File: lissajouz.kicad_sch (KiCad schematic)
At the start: 105 parts, among them J1 Barrel_Jack, Q1 BC557, Q10 2N7000, Q2 BC557, Q3 2N7000, Q4 BC557, Q5 BC557, Q6 2N7000, Q7 2N7000, Q8 2N7000, Q9 2N7000, U1 LM324, U2 LM324, U3 LM324

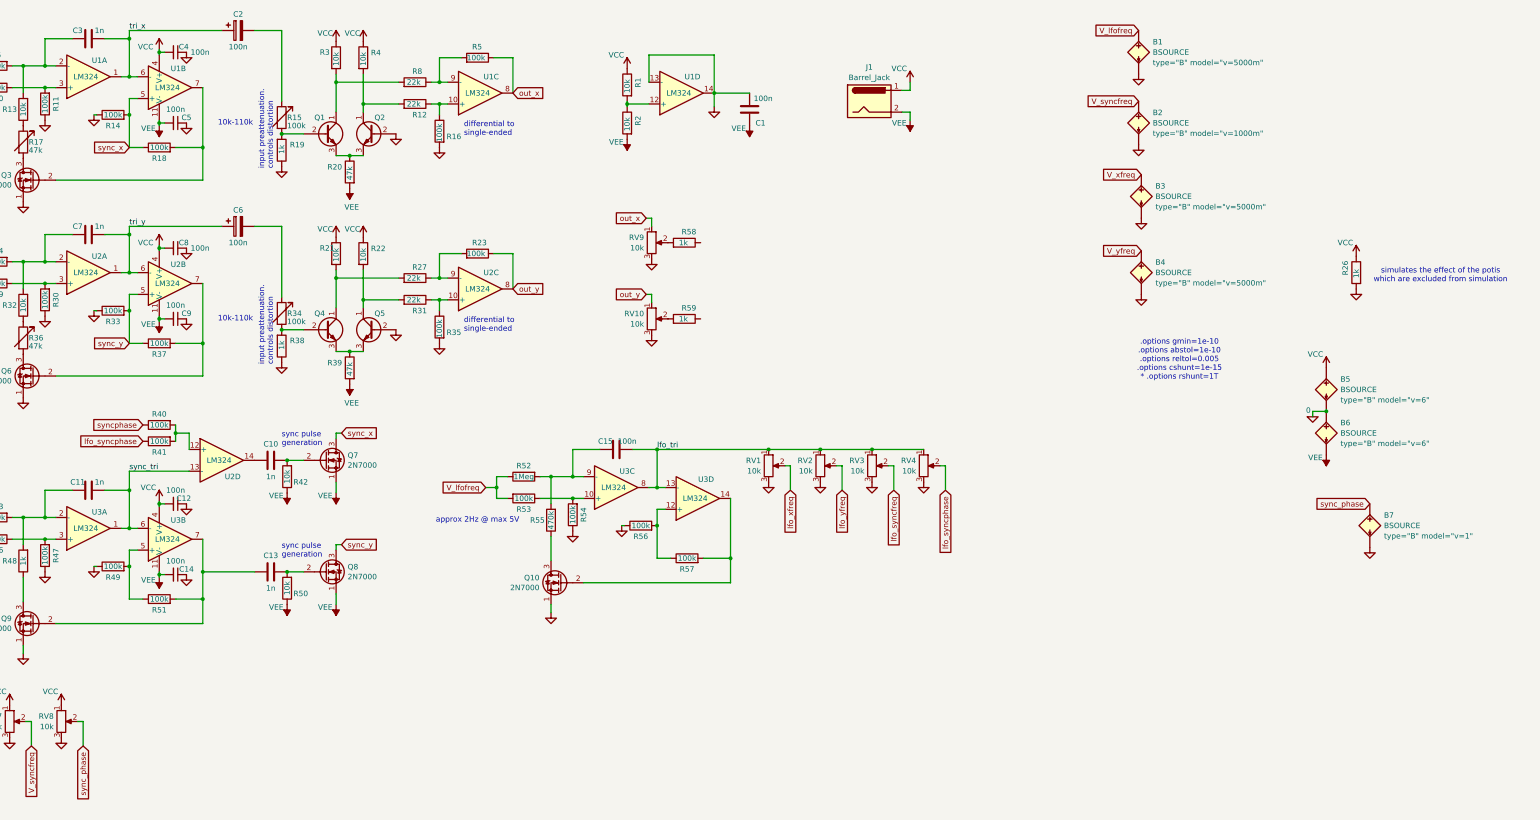
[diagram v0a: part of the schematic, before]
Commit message: add most footprints
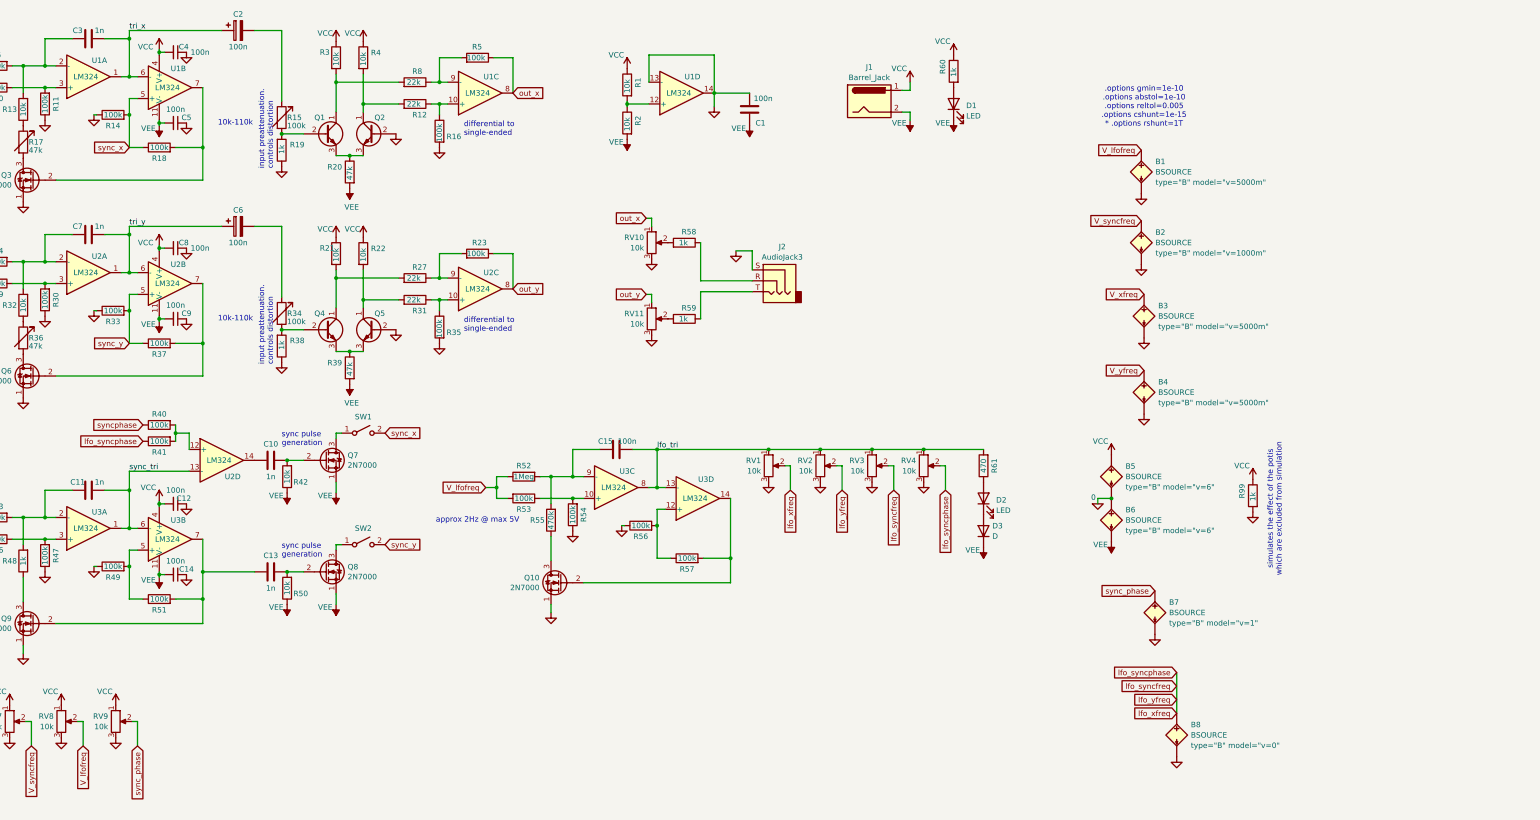
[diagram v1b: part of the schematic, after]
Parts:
- added B8: BSOURCE, symbol Simulation_SPICE:BSOURCE
- added D1, D2: LED, LED_THT:LED_D3.0mm, symbol Device:LED
- added D3: D, Diode_THT:D_5W_P5.08mm_Vertical_AnodeUp, symbol Device:D
- added J2: AudioJack3, symbol Connector_Audio:AudioJack3
- added R60: 1k, Resistor_SMD:R_0805_2012Metric_Pad1.20x1.40mm_HandSolder, symbol Device:R
- added R61: 470, Resistor_SMD:R_0805_2012Metric_Pad1.20x1.40mm_HandSolder, symbol Device:R
- added RV9: 10k, Potentiometer_THT:Potentiometer_Alpha_RD901F-40-00D_Single_Vertical, symbol Device:R_Potentiometer
- added SW1, SW2: ${SIM.PARAMS}, symbol Switch:SW_SPST
- C1, C10, C11, C12, C13, C14, C15, C3, C4, C5, C7, C8, C9: footprint Capacitor_SMD:C_0805_2012Metric_Pad1.15x1.40mm_HandSolder -> Capacitor_SMD:C_0805_2012Metric_Pad1.18x1.45mm_HandSolder
- C2, C6: footprint Capacitor_THT:CP_Radial_D7.5mm_P2.50mm -> Capacitor_SMD:C_0805_2012Metric_Pad1.18x1.45mm_HandSolder
- J1: footprint (none) -> Connector_BarrelJack:BarrelJack_SwitchcraftConxall_RAPC10U_Horizontal
- R1, R10, R11, R12, R13, R14, R16, R18, R19, R2, R20, R21, R22, R23, R24, R25, R27, R28, R29, R3, R30, R31, R32, R33, R35, R37, R38, R39, R4, R40, R41, R42, R43, R44, R45, R46, R47, R48, R49, R5, R50, R51, R52, R53, R54, R55, R56, R57, R58, R59, R6, R7, R8, R9: footprint Resistor_SMD:R_0805_2012Metric_Pad1.15x1.40mm_HandSolder -> Resistor_SMD:R_0805_2012Metric_Pad1.20x1.40mm_HandSolder
- R15, R34: footprint Potentiometer_THT:Potentiometer_Runtron_RM-065_Vertical -> Potentiometer_THT:Potentiometer_Alpha_RD901F-40-00D_Single_Vertical
- R17, R36: footprint Potentiometer_THT:Potentiometer_Runtron_RM-065_Vertical -> Resistor_SMD:R_0805_2012Metric_Pad1.20x1.40mm_HandSolder
- RV1, RV2, RV3, RV4, RV5, RV6, RV7, RV8: footprint (none) -> Potentiometer_THT:Potentiometer_Alpha_RD901F-40-00D_Single_Vertical
- RV10: renamed from RV9; footprint (none) -> Potentiometer_THT:Potentiometer_Runtron_RM-065_Vertical
- RV11: renamed from RV10; footprint (none) -> Potentiometer_THT:Potentiometer_Runtron_RM-065_Vertical
- renumbered R26 to R99
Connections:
- net lfo_syncphase is gone; now on net lfo_syncfreq: R41.1, RV4.2
- net lfo_xfreq is gone; now on net lfo_syncfreq: R9.1, RV1.2
- net lfo_yfreq is gone; now on net lfo_syncfreq: R28.1, RV2.2
- net GNDREF: now also B8.2 (N-), J2.S, RV9.3
- net VCC: now also R60.1, RV9.1
- net VEE: now also D1.1 (K), D3.1 (K)
- net V_lfofreq: now also RV8.2
- net lfo_syncfreq: now also B8.1 (N+)
- net lfo_tri: now also R61.2
- net sync_phase: now also RV9.2; no longer RV8.2
- net sync_x: now also SW1.2 (B); no longer Q7.3 (D)
- net sync_y: now also SW2.2 (B); no longer Q8.3 (D)
- net at R59.1: now also J2.T
- net at R58.1: now also J2.R
- new net: D2.1 (K), D3.2 (A)
- new net: D2.2 (A), R61.1
- new net: Q7.3 (D), SW1.1 (A)
- new net: Q8.3 (D), SW2.1 (A)
- new net: D1.2 (A), R60.2
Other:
- moved on the sheet: B1, B2, B3, B4, B5, B6, B7, R99

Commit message: pcb
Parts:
- R17, R36: footprint Resistor_SMD:R_0805_2012Metric_Pad1.20x1.40mm_HandSolder -> Potentiometer_THT:Potentiometer_Alpha_RD901F-40-00D_Single_Vertical
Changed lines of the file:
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@@
 			)
 		)
-		(property "Footprint" "Resistor_SMD:R_0805_2012Metric_Pad1.20x1.40mm_HandSolder"
+		(property "Footprint" "Potentiometer_THT:Potentiometer_Alpha_RD901F-40-00D_Single_Vertical"
 			(at 48.387 86.995 90)
 			(effects
@@
 			)
 		)
-		(property "Footprint" "Resistor_SMD:R_0805_2012Metric_Pad1.20x1.40mm_HandSolder"
+		(property "Footprint" "Potentiometer_THT:Potentiometer_Alpha_RD901F-40-00D_Single_Vertical"
 			(at 48.387 41.275 90)
 			(effects

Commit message: kinda final-ish UI layout
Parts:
- added R26, R62: 100k, Resistor_SMD:R_0805_2012Metric_Pad1.20x1.40mm_HandSolder, symbol Device:R
- added R63, R64, R65: 1k, Resistor_SMD:R_0805_2012Metric_Pad1.20x1.40mm_HandSolder, symbol Device:R
- added R66: 2.2k, Resistor_SMD:R_0805_2012Metric_Pad1.20x1.40mm_HandSolder, symbol Device:R
- added R67, R68: 4.7k, Resistor_SMD:R_0805_2012Metric_Pad1.20x1.40mm_HandSolder, symbol Device:R
- added R69: 1Meg, Resistor_SMD:R_0805_2012Metric_Pad1.20x1.40mm_HandSolder, symbol Device:R
- added RV12, RV13, RV14: 10k, Potentiometer_THT:Potentiometer_Alpha_RD901F-40-00D_Single_Vertical, symbol Device:R_Potentiometer
- J1: footprint Connector_BarrelJack:BarrelJack_SwitchcraftConxall_RAPC10U_Horizontal -> footprints:myBarrelJack
- J2: footprint (none) -> Connector_Audio:Jack_3.5mm_CUI_SJ1-3535NG_Horizontal
- SW1, SW2: footprint (none) -> footprints:switch8x8
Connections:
- net syncphase is gone; now on net sync_phase: R40.1
- net GNDREF: now also R63.1, R64.1, R65.1, R66.1, RV12.3, RV13.3; no longer RV5.3, RV6.3, RV7.3, RV8.3, RV9.3
- net VCC: now also R67.2, RV12.1, RV13.1, RV14.1; no longer RV9.1
- net VEE: now also R68.1, RV14.3
- net at R40.2, R41.2, U2.12 (+): now also R69.2
- net at R24.1, R25.2, R28.2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: now also R62.2
- net at R10.2, R6.1, R7.2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: now also R26.2
- new net: R64.2, RV6.3
- new net: R67.1, RV9.1
- new net: R68.2, RV9.3
- new net: R66.2, RV8.3
- new net: R65.2, RV7.3
- new net: R63.2, RV5.3
- new net V_xfreq_fine: R26.1, RV12.2
- new net V_yfreq_fine: R62.1, RV13.2
- new net sync_phase_fine: R69.1, RV14.2
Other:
- moved on the sheet: R25, R28, R40, R7, R9, RV7, RV8, RV9

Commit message: all components positioned
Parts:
- added B10, B11, B9: BSOURCE, symbol Simulation_SPICE:BSOURCE
- D3: footprint Diode_THT:D_5W_P5.08mm_Vertical_AnodeUp -> Diode_THT:D_5W_P12.70mm_Horizontal
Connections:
- net GNDREF is gone; now on net GND: B1.2 (N-), B2.2 (N-), B3.2 (N-), B4.2 (N-), B7.2 (N-), B8.2 (N-), C1.1, C12.1, C14.1, C4.1, C5.1, C8.1, C9.1, J2.S, Q10.1 (S), Q3.1 (S), Q6.1 (S), Q9.1 (S), R11.1, R14.1, R30.1, R33.1, R47.1, R49.1, R54.1, R56.1, R63.1, R64.1, R65.1, R66.1, R99.2, RV1.3, RV10.3, RV11.3, RV12.3, RV13.3, RV2.3, RV3.3, RV4.3, U1.13 (-), U1.14
- net GND: now also B10.2 (N-), B11.2 (N-), B9.2 (N-)
- net V_xfreq: now also R25.1; no longer R7.1
- net V_xfreq_fine: now also R62.1; no longer R26.1
- net V_yfreq: now also R7.1; no longer R25.1
- net V_yfreq_fine: now also R26.1; no longer R62.1
- net lfo_syncfreq: now also B10.1 (N+); no longer B8.1 (N+), R28.1, R41.1, R9.1, RV1.2, RV2.2, RV4.2
- net lfo_tri: now also U3.6 (-); no longer U3.13 (-)
- net out_x: now also R23.1, U2.8; no longer R5.1, U1.8
- net out_y: now also R5.1, U1.8; no longer R23.1, U2.8
- net sync_tri: now also U3.13 (-); no longer U3.6 (-)
- net sync_x: now also R33.2, R37.1, U2.5 (+); no longer R14.2, R18.1, U1.5 (+)
- net sync_y: now also R14.2, R18.1, U1.5 (+); no longer R33.2, R37.1, U2.5 (+)
- net tri_x: now also C6.1, C7.1, U2.1, U2.6 (-); no longer C2.1, C3.1, U1.1, U1.6 (-)
- net tri_y: now also C2.1, C3.1, U1.1, U1.6 (-); no longer C6.1, C7.1, U2.1, U2.6 (-)
- net at R49.2, R51.1: now also U3.12 (+); no longer U3.5 (+)
- net at C13.2, Q9.2 (G), R51.2: now also U3.14; no longer U3.7
- net at R56.2, R57.1: now also U3.5 (+); no longer U3.12 (+)
- net at Q10.2 (G), R57.2: now also U3.7; no longer U3.14
- new net lfo_syncphase: B11.1 (N+), R41.1, RV4.2
- new net lfo_xfreq: B8.1 (N+), R28.1, RV1.2
- new net lfo_yfreq: B9.1 (N+), R9.1, RV2.2
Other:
- moved on the sheet: B8

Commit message: frontplate++
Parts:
- added R70, R71: 10k, Resistor_SMD:R_0805_2012Metric_Pad1.20x1.40mm_HandSolder, symbol Device:R
- R15, R17, R34, R36, RV1, RV12, RV13, RV14, RV2, RV3, RV4, RV5, RV6, RV7, RV8, RV9: footprint Potentiometer_THT:Potentiometer_Alpha_RD901F-40-00D_Single_Vertical -> footprints:my_poti_Potentiometer_Alpha_RD901F-40-00D_Single_Vertical
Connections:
- net at C6.2: now also R71.2; no longer R34.1
- net at R15.1: now also R70.1; no longer C2.2
- new net: C2.2, R70.2
- new net: R34.1, R71.1
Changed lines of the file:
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@@
 	(wire
 		(pts
-			(xy 110.49 15.24) (xy 110.49 31.75)
-		)
-		(stroke
-			(width 0)
-			(type default)
-		)
-	)
-	(wire
-		(pts
 			(xy 229.235 122.555) (xy 229.235 116.84)
 		)
@@
 	(wire
 		(pts
+			(xy 110.49 15.24) (xy 110.49 24.13)
+		)
+		(stroke
+			(width 0)
+			(type default)
+		)
+	)
+	(wire
+		(pts
 			(xy 61.595 62.865) (xy 55.245 62.865)
 		)
@@
 	(wire
 		(pts
+			(xy 110.49 60.96) (xy 110.49 69.85)
+		)
+		(stroke
+			(width 0)
+			(type default)
+		)
+	)
+	(wire
+		(pts
 			(xy 229.235 116.84) (xy 227.965 116.84)
 		)
@@
 	(wire
 		(pts
-			(xy 110.49 60.96) (xy 110.49 77.47)
-		)
-		(stroke
-			(width 0)
-			(type default)
-		)
-	)
-	(wire
-		(pts
 			(xy 164.465 21.59) (xy 164.465 29.845)
 		)
@@
 		(on_board yes)
 		(dnp no)
-		(fields_autoplaced yes)
 		(property "Reference" "RV4"
 			(at 258.5721 115.6278 0)
@@
 			)
 		)
-		(property "Footprint" "Potentiometer_THT:Potentiometer_Alpha_RD901F-40-00D_Single_Vertical"
+		(property "Footprint" "footprints:my_poti_Potentiometer_Alpha_RD901F-40-00D_Single_Vertical"
 			(at 260.35 116.84 0)
 			(effects
@@
 	)
 	(symbol
+		(lib_id "Device:R")
+		(at 110.49 27.94 0)
+		(mirror x)
+		(unit 1)
+		(exclude_from_sim no)
+		(in_bom yes)
+		(on_board yes)
+		(dnp no)
+		(property "Reference" "R70"
+			(at 112.395 26.67 0)
+			(effects
+				(font
+					(size 1.27 1.27)
+				)
+				(justify left)
+			)
+		)
+		(property "Value" "10k"
+			(at 110.49 26.035 90)
+			(effects
+				(font
+					(size 1.27 1.27)
+				)
+				(justify left)
+			)
+		)
+		(property "Footprint" "Resistor_SMD:R_0805_2012Metric_Pad1.20x1.40mm_HandSolder"
+			(at 108.712 27.94 90)
+			(effects
+				(font
+					(size 1.27 1.27)
+				)
+				(hide yes)
+			)
+		)
+		(property "Datasheet" "~"
+			(at 110.49 27.94 0)
+			(effects
+				(font
+					(size 1.27 1.27)
+				)
+				(hide yes)
+			)
+		)
+		(property "Description" ""
+			(at 110.49 27.94 0)
+			(effects
+				(font
+					(size 1.27 1.27)
+				)
+				(hide yes)
+			)
+		)
+		(pin "1"
+		)
+		(pin "2"
+		)
+		(instances
+			(project "lissajouz"
+				(path "/411c8e98-f01c-4ee2-9630-e2b01df2741b"
+					(reference "R70")
+					(unit 1)
+				)
+			)
+		)
+	)
+	(symbol
 		(lib_id "Amplifier_Operational:LM324")
 		(at 84.455 133.985 0)
@@
 			)
 		)
-		(property "Footprint" "Potentiometer_THT:Potentiometer_Alpha_RD901F-40-00D_Single_Vertical"
+		(property "Footprint" "footprints:my_poti_Potentiometer_Alpha_RD901F-40-00D_Single_Vertical"
 			(at 108.712 35.56 90)
 			(effects
@@
 		(on_board yes)
 		(dnp no)
-		(fields_autoplaced yes)
 		(property "Reference" "RV14"
 			(at 107.4421 175.3178 0)
@@
 			)
 		)
-		(property "Footprint" "Potentiometer_THT:Potentiometer_Alpha_RD901F-40-00D_Single_Vertical"
+		(property "Footprint" "footprints:my_poti_Potentiometer_Alpha_RD901F-40-00D_Single_Vertical"
 			(at 109.22 176.53 0)
 			(effects
@@
 		(dnp no)
 		(property "Reference" "R21"
-			(at 119.38 66.04 0)
+			(at 117.475 66.04 0)
 			(effects
 				(font
@@
 		(on_board yes)
 		(dnp no)
-		(fields_autoplaced yes)
 		(property "Reference" "RV2"
 			(at 234.4421 115.6278 0)
@@
 			)
 		)
-		(property "Footprint" "Potentiometer_THT:Potentiometer_Alpha_RD901F-40-00D_Single_Vertical"
+		(property "Footprint" "footprints:my_poti_Potentiometer_Alpha_RD901F-40-00D_Single_Vertical"
 			(at 236.22 116.84 0)
 			(effects
@@
 		(on_board yes)
 		(dnp no)
-		(fields_autoplaced yes)
 		(property "Reference" "RV9"
 			(at 94.7421 175.3178 0)
@@
 			)
 		)
-		(property "Footprint" "Potentiometer_THT:Potentiometer_Alpha_RD901F-40-00D_Single_Vertical"
+		(property "Footprint" "footprints:my_poti_Potentiometer_Alpha_RD901F-40-00D_Single_Vertical"
 			(at 96.52 176.53 0)
 			(effects
@@
 		(on_board yes)
 		(dnp no)
-		(fields_autoplaced yes)
 		(property "Reference" "RV12"
 			(at 45.8471 175.3178 0)
@@
 			)
 		)
-		(property "Footprint" "Potentiometer_THT:Potentiometer_Alpha_RD901F-40-00D_Single_Vertical"
+		(property "Footprint" "footprints:my_poti_Potentiometer_Alpha_RD901F-40-00D_Single_Vertical"
 			(at 47.625 176.53 0)
 			(effects
@@
 			)
 		)
-		(property "Footprint" "Potentiometer_THT:Potentiometer_Alpha_RD901F-40-00D_Single_Vertical"
+		(property "Footprint" "footprints:my_poti_Potentiometer_Alpha_RD901F-40-00D_Single_Vertical"
 			(at 48.387 86.995 90)
 			(effects
@@
 		(on_board yes)
 		(dnp no)
-		(fields_autoplaced yes)
 		(property "Reference" "RV1"
 			(at 222.3771 115.6278 0)
@@
 			)
 		)
-		(property "Footprint" "Potentiometer_THT:Potentiometer_Alpha_RD901F-40-00D_Single_Vertical"
+		(property "Footprint" "footprints:my_poti_Potentiometer_Alpha_RD901F-40-00D_Single_Vertical"
 			(at 224.155 116.84 0)
 			(effects
@@
 			)
 		)
-		(property "Footprint" "Potentiometer_THT:Potentiometer_Alpha_RD901F-40-00D_Single_Vertical"
+		(property "Footprint" "footprints:my_poti_Potentiometer_Alpha_RD901F-40-00D_Single_Vertical"
 			(at 48.387 41.275 90)
 			(effects
@@
 		(on_board yes)
 		(dnp no)
-		(fields_autoplaced yes)
 		(property "Reference" "RV10"
-			(at 195.072 63.5578 0)
+			(at 194.945 63.5 0)
 			(effects
 				(font
@@
 		)
 		(property "Value" "10k"
-			(at 195.072 65.9821 0)
+			(at 194.945 66.04 0)
 			(effects
 				(font
@@
 		(on_board yes)
 		(dnp no)
-		(fields_autoplaced yes)
 		(property "Reference" "RV8"
 			(at 82.0421 175.3178 0)
@@
 			)
 		)
-		(property "Footprint" "Potentiometer_THT:Potentiometer_Alpha_RD901F-40-00D_Single_Vertical"
+		(property "Footprint" "footprints:my_poti_Potentiometer_Alpha_RD901F-40-00D_Single_Vertical"
 			(at 83.82 176.53 0)
 			(effects
@@
 		(on_board yes)
 		(dnp no)
-		(fields_autoplaced yes)
 		(property "Reference" "RV7"
 			(at 69.9771 175.3178 0)
@@
 			)
 		)
-		(property "Footprint" "Potentiometer_THT:Potentiometer_Alpha_RD901F-40-00D_Single_Vertical"
+		(property "Footprint" "footprints:my_poti_Potentiometer_Alpha_RD901F-40-00D_Single_Vertical"
 			(at 71.755 176.53 0)
 			(effects
@@
 		(on_board yes)
 		(dnp no)
-		(fields_autoplaced yes)
 		(property "Reference" "RV13"
 			(at 57.9121 175.3178 0)
@@
 			)
 		)
-		(property "Footprint" "Potentiometer_THT:Potentiometer_Alpha_RD901F-40-00D_Single_Vertical"
+		(property "Footprint" "footprints:my_poti_Potentiometer_Alpha_RD901F-40-00D_Single_Vertical"
 			(at 59.69 176.53 0)
 			(effects
@@
 			)
 		)
-		(property "Footprint" "Potentiometer_THT:Potentiometer_Alpha_RD901F-40-00D_Single_Vertical"
+		(property "Footprint" "footprints:my_poti_Potentiometer_Alpha_RD901F-40-00D_Single_Vertical"
 			(at 108.712 81.28 90)
 			(effects
@@
 		(on_board yes)
 		(dnp no)
-		(fields_autoplaced yes)
 		(property "Reference" "RV5"
 			(at 21.0821 175.3178 0)
@@
 			)
 		)
-		(property "Footprint" "Potentiometer_THT:Potentiometer_Alpha_RD901F-40-00D_Single_Vertical"
+		(property "Footprint" "footprints:my_poti_Potentiometer_Alpha_RD901F-40-00D_Single_Vertical"
 			(at 22.86 176.53 0)
 			(effects
@@
 		(on_board yes)
 		(dnp no)
-		(fields_autoplaced yes)
 		(property "Reference" "RV6"
 			(at 33.1471 175.3178 0)
@@
 			)
 		)
-		(property "Footprint" "Potentiometer_THT:Potentiometer_Alpha_RD901F-40-00D_Single_Vertical"
+		(property "Footprint" "footprints:my_poti_Potentiometer_Alpha_RD901F-40-00D_Single_Vertical"
 			(at 34.925 176.53 0)
 			(effects
@@
 		(on_board yes)
 		(dnp no)
-		(fields_autoplaced yes)
 		(property "Reference" "RV3"
 			(at 246.5071 115.6278 0)
@@
 			)
 		)
-		(property "Footprint" "Potentiometer_THT:Potentiometer_Alpha_RD901F-40-00D_Single_Vertical"
+		(property "Footprint" "footprints:my_poti_Potentiometer_Alpha_RD901F-40-00D_Single_Vertical"
 			(at 248.285 116.84 0)
 			(effects
@@
 	(symbol
 		(lib_id "Device:R")
+		(at 110.49 73.66 0)
+		(mirror x)
+		(unit 1)
+		(exclude_from_sim no)
+		(in_bom yes)
+		(on_board yes)
+		(dnp no)
+		(property "Reference" "R71"
+			(at 112.395 72.39 0)
+			(effects
+				(font
+					(size 1.27 1.27)
+				)
+				(justify left)
+			)
+		)
+		(property "Value" "10k"
+			(at 110.49 71.755 90)
+			(effects
+				(font
+					(size 1.27 1.27)
+				)
+				(justify left)
+			)
+		)
+		(property "Footprint" "Resistor_SMD:R_0805_2012Metric_Pad1.20x1.40mm_HandSolder"
+			(at 108.712 73.66 90)
+			(effects
+				(font
+					(size 1.27 1.27)
+				)
+				(hide yes)
+			)
+		)
+		(property "Datasheet" "~"
+			(at 110.49 73.66 0)
+			(effects
+				(font
+					(size 1.27 1.27)
+				)
+				(hide yes)
+			)
+		)
+		(property "Description" ""
+			(at 110.49 73.66 0)
+			(effects
+				(font
+					(size 1.27 1.27)
+				)
+				(hide yes)
+			)
+		)
+		(pin "1"
+		)
+		(pin "2"
+		)
+		(instances
+			(project "lissajouz"
+				(path "/411c8e98-f01c-4ee2-9630-e2b01df2741b"
+					(reference "R71")
+					(unit 1)
+				)
+			)
+		)
+	)
+	(symbol
+		(lib_id "Device:R")
 		(at 129.54 67.31 0)
 		(unit 1)
@@
 		(dnp no)
 		(property "Reference" "RV11"
-			(at 195.0721 81.3378 0)
+			(at 194.945 81.28 0)
 			(effects
 				(font
@@
 		)
 		(property "Value" "10k"
-			(at 195.0721 83.7621 0)
+			(at 194.945 83.82 0)
 			(effects
 				(font
